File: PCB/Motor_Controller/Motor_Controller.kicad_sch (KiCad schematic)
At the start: 6 parts, among them J1 Motor, Q1 FQD50N06

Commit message: PCB and PWM Update
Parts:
- added D2: IR204A, LED_THT:LED_D3.0mm_IRBlack, symbol LED:IR204A
- added U1: QSE159, OptoDevice:ONSemi_QSE15x, symbol Interface_Optical:QSE159
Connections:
- net GND: now also R2.2; no longer Q1.3 (S), R1.2
- net VIN_12V: now also D1.1 (K), J1.1 (Pin_1); no longer R2.1
- new net ISENSE: Q1.3 (S), R1.2, R2.1
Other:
- moved on the sheet: R2

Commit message: PCB Update
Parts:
- added U2: CH32V003FxPx, Package_SO:TSSOP-20_4.4x6.5mm_P0.65mm, symbol MCU_WCH_CH32V0:CH32V003FxPx
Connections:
- net GND: now also U2.7 (VSS)
- new net CONTROL_POT: U2.20 (PD3)
- new net ISENSE_AMPED: U2.1 (PD4)
- new net MOTOR_PWM: U2.10 (PC0)
- new net NRST: U2.4 (PD7)
- new net VIN_3V3: U2.9 (VDD)

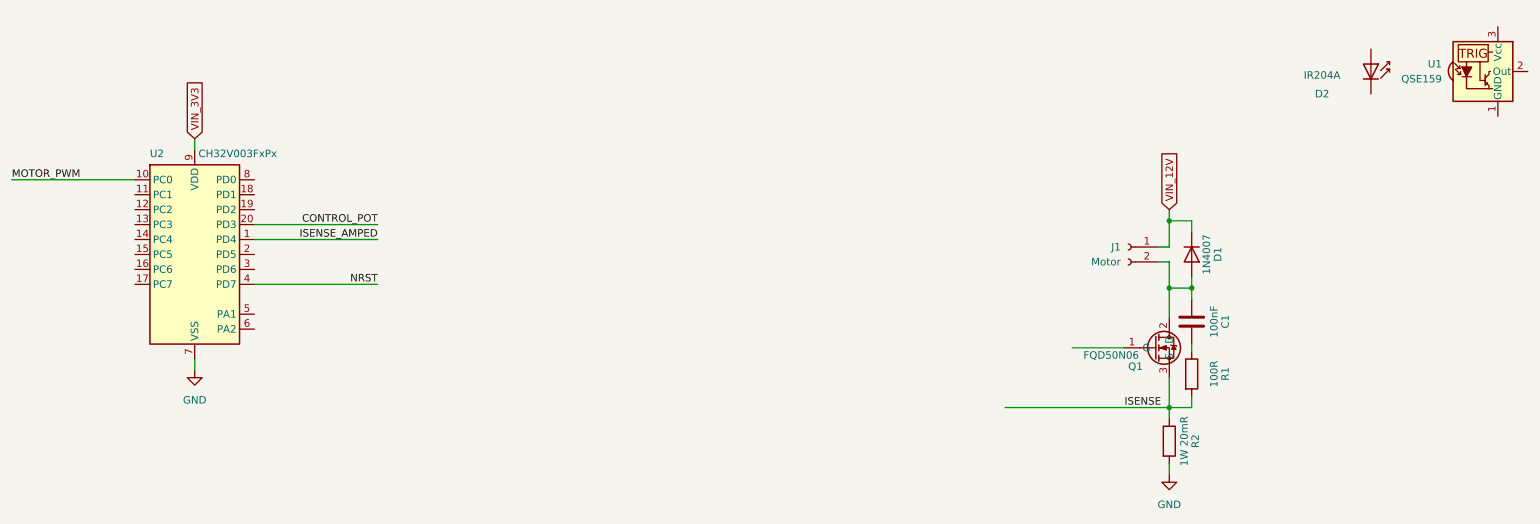
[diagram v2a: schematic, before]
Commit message: Op-Amp Specific Testing
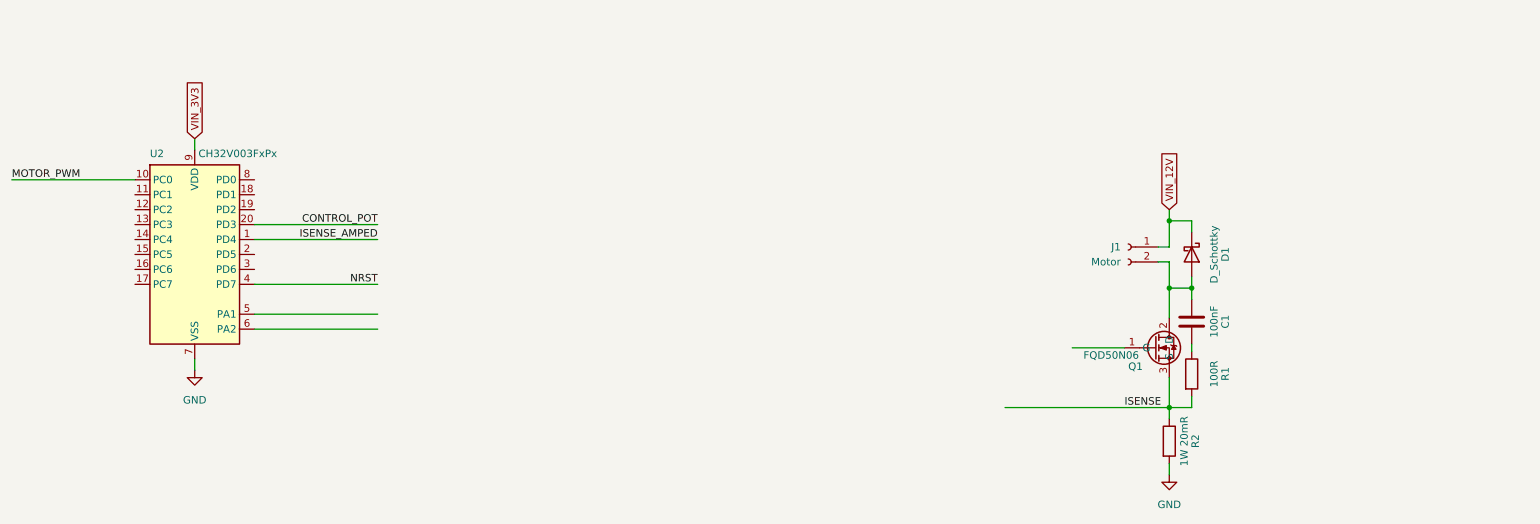
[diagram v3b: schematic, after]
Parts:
- removed D1: 1N4007, symbol Device:D
- removed D2: IR204A, LED_THT:LED_D3.0mm_IRBlack, symbol LED:IR204A
- removed U1: QSE159, OptoDevice:ONSemi_QSE15x, symbol Interface_Optical:QSE159
- added D1: D_Schottky, symbol Device:D_Schottky
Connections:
- net VIN_12V: now also D1.1 (K)
- net at C1.1, J1.2 (Pin_2), Q1.2 (D): now also D1.2 (A)
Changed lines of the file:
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@@
+	(wire
+		(pts
+			(xy 66.04 67.945) (xy 86.995 67.945)
+		)
+		(stroke
+			(width 0)
+			(type default)
+		)
+	)
 	(wire
 		(pts
@@
 		(pts
 			(xy 225.425 51.435) (xy 225.425 49.53)
+		)
+		(stroke
+			(width 0)
+			(type default)
+		)
+	)
+	(wire
+		(pts
+			(xy 66.04 65.405) (xy 86.995 65.405)
 		)
 		(stroke
@@
 	)
 	(symbol
-		(lib_id "Interface_Optical:QSE159")
-		(at 274.955 24.13 0)
-		(unit 1)
-		(exclude_from_sim no)
-		(in_bom yes)
-		(on_board yes)
-		(dnp no)
-		(fields_autoplaced yes)
-		(property "Reference" "U1"
-			(at 267.97 22.8599 0)
-			(effects
-				(font
-					(size 1.27 1.27)
-				)
-				(justify right)
-			)
-		)
-		(property "Value" "QSE159"
-			(at 267.97 25.3999 0)
-			(effects
-				(font
-					(size 1.27 1.27)
-				)
-				(justify right)
-			)
-		)
-		(property "Footprint" "OptoDevice:ONSemi_QSE15x"
-			(at 274.955 34.29 0)
-			(effects
-				(font
-					(size 1.27 1.27)
-				)
-				(hide yes)
-			)
-		)
-		(property "Datasheet" "http://www.onsemi.com/pub/Collateral/QSE159-D.pdf"
-			(at 291.465 16.51 0)
-			(effects
-				(font
-					(size 1.27 1.27)
-				)
-				(hide yes)
-			)
-		)
-		(property "Description" "Plastic Silicon Photosensor"
-			(at 274.955 24.13 0)
-			(effects
-				(font
-					(size 1.27 1.27)
-				)
-				(hide yes)
-			)
-		)
-		(pin "3"
-		)
-		(pin "1"
-		)
-		(pin "2"
-		)
-		(instances
-			(project ""
-				(path "/75427121-ba70-43d0-b78e-325c2cfaa959"
-					(reference "U1")
-					(unit 1)
-				)
-			)
-		)
-	)
-	(symbol
-		(lib_id "Device:D")
-		(at 225.425 55.245 270)
-		(unit 1)
-		(exclude_from_sim no)
-		(in_bom yes)
-		(on_board yes)
-		(dnp no)
-		(property "Reference" "D1"
-			(at 229.87 55.245 0)
-			(effects
-				(font
-					(size 1.27 1.27)
-				)
-			)
-		)
-		(property "Value" "1N4007"
-			(at 227.965 55.245 0)
-			(effects
-				(font
-					(size 1.27 1.27)
-				)
-			)
-		)
-		(property "Footprint" ""
-			(at 225.425 55.245 0)
-			(effects
-				(font
-					(size 1.27 1.27)
-				)
-				(hide yes)
-			)
-		)
-		(property "Datasheet" "~"
-			(at 225.425 55.245 0)
-			(effects
-				(font
-					(size 1.27 1.27)
-				)
-				(hide yes)
-			)
-		)
-		(property "Description" "Diode"
-			(at 225.425 55.245 0)
-			(effects
-				(font
-					(size 1.27 1.27)
-				)
-				(hide yes)
-			)
-		)
-		(property "Sim.Device" "D"
-			(at 225.425 55.245 0)
-			(effects
-				(font
-					(size 1.27 1.27)
-				)
-				(hide yes)
-			)
-		)
-		(property "Sim.Pins" "1=K 2=A"
-			(at 225.425 55.245 0)
-			(effects
-				(font
-					(size 1.27 1.27)
-				)
-				(hide yes)
-			)
-		)
-		(pin "1"
-		)
-		(pin "2"
-		)
-		(instances
-			(project ""
-				(path "/75427121-ba70-43d0-b78e-325c2cfaa959"
-					(reference "D1")
-					(unit 1)
-				)
-			)
-		)
-	)
-	(symbol
 		(lib_id "Connector:Conn_01x02_Socket")
 		(at 214.63 53.975 0)
@@
 	)
 	(symbol
-		(lib_id "LED:IR204A")
-		(at 255.905 22.86 270)
-		(mirror x)
+		(lib_id "Device:D_Schottky")
+		(at 225.425 55.245 270)
 		(unit 1)
 		(exclude_from_sim no)
@@
 		(on_board yes)
 		(dnp no)
-		(property "Reference" "D2"
-			(at 246.38 27.94 90)
-			(effects
-				(font
-					(size 1.27 1.27)
-				)
-				(justify left)
-			)
-		)
-		(property "Value" "IR204A"
-			(at 244.475 24.765 90)
-			(effects
-				(font
-					(size 1.27 1.27)
-				)
-				(justify left)
-			)
-		)
-		(property "Footprint" "LED_THT:LED_D3.0mm_IRBlack"
-			(at 260.35 22.86 0)
-			(effects
-				(font
-					(size 1.27 1.27)
-				)
-				(hide yes)
-			)
-		)
-		(property "Datasheet" "http://www.everlight.com/file/ProductFile/IR204-A.pdf"
-			(at 255.905 24.13 0)
-			(effects
-				(font
-					(size 1.27 1.27)
-				)
-				(hide yes)
-			)
-		)
-		(property "Description" "Infrared LED , 3mm LED package"
-			(at 255.905 22.86 0)
-			(effects
-				(font
-					(size 1.27 1.27)
-				)
-				(hide yes)
-			)
+		(property "Reference" "D1"
+			(at 231.14 55.245 0)
+			(effects
+				(font
+					(size 1.27 1.27)
+				)
+			)
+		)
+		(property "Value" "D_Schottky"
+			(at 229.235 55.245 0)
+			(effects
+				(font
+					(size 1.27 1.27)
+				)
+			)
+		)
+		(property "Footprint" ""
+			(at 225.425 55.245 0)
+			(effects
+				(font
+					(size 1.27 1.27)
+				)
+				(hide yes)
+			)
+		)
+		(property "Datasheet" "~"
+			(at 225.425 55.245 0)
+			(effects
+				(font
+					(size 1.27 1.27)
+				)
+				(hide yes)
+			)
+		)
+		(property "Description" "Schottky diode"
+			(at 225.425 55.245 0)
+			(effects
+				(font
+					(size 1.27 1.27)
+				)
+				(hide yes)
+			)
+		)
+		(pin "1"
 		)
 		(pin "2"
-		)
-		(pin "1"
 		)
 		(instances
 			(project ""
 				(path "/75427121-ba70-43d0-b78e-325c2cfaa959"
-					(reference "D2")
+					(reference "D1")
 					(unit 1)
 				)

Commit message: Added Op Amp code
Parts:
- added R3: 4K7, symbol Device:R
- added R4: 220R, symbol Device:R
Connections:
- net GND: now also R4.2
- net ISENSE_AMPED: now also R3.1
- net at U2.5 (PA1): now also R3.2, R4.1
- net ISENSE_LV: now reaches U2.6 (PA2)
- net ISENSE: no longer names the net of Q1.3 (S), R1.2, R2.1

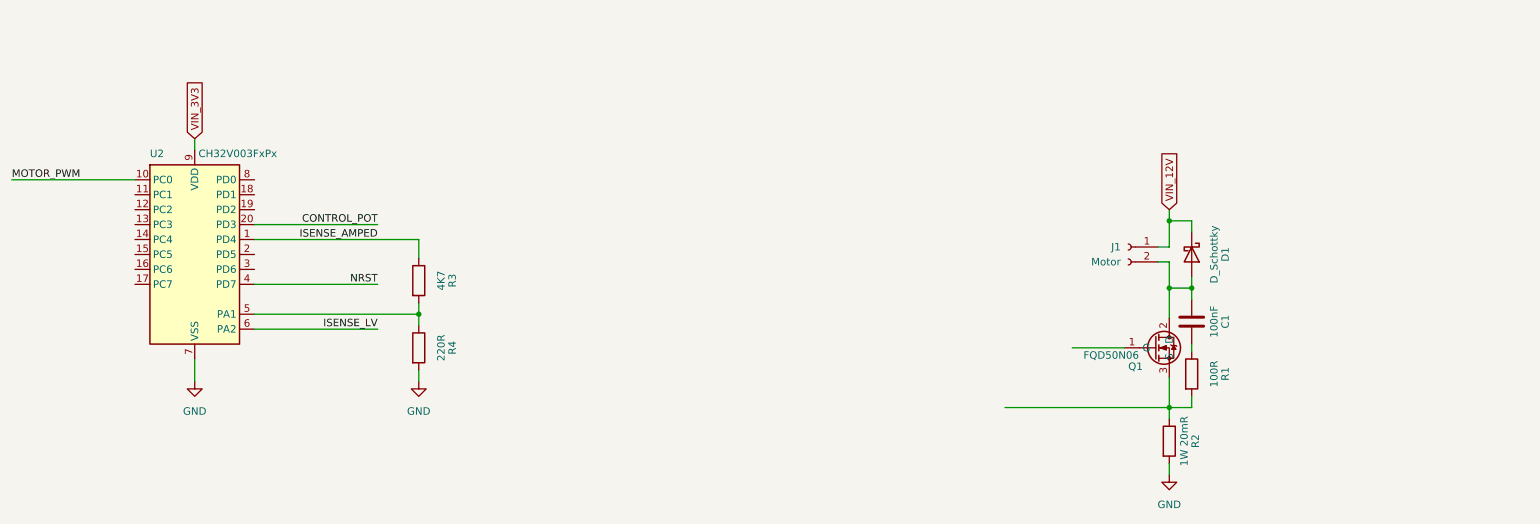
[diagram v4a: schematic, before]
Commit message: Removed Mosfet Driver. Using discreet Push-Pull
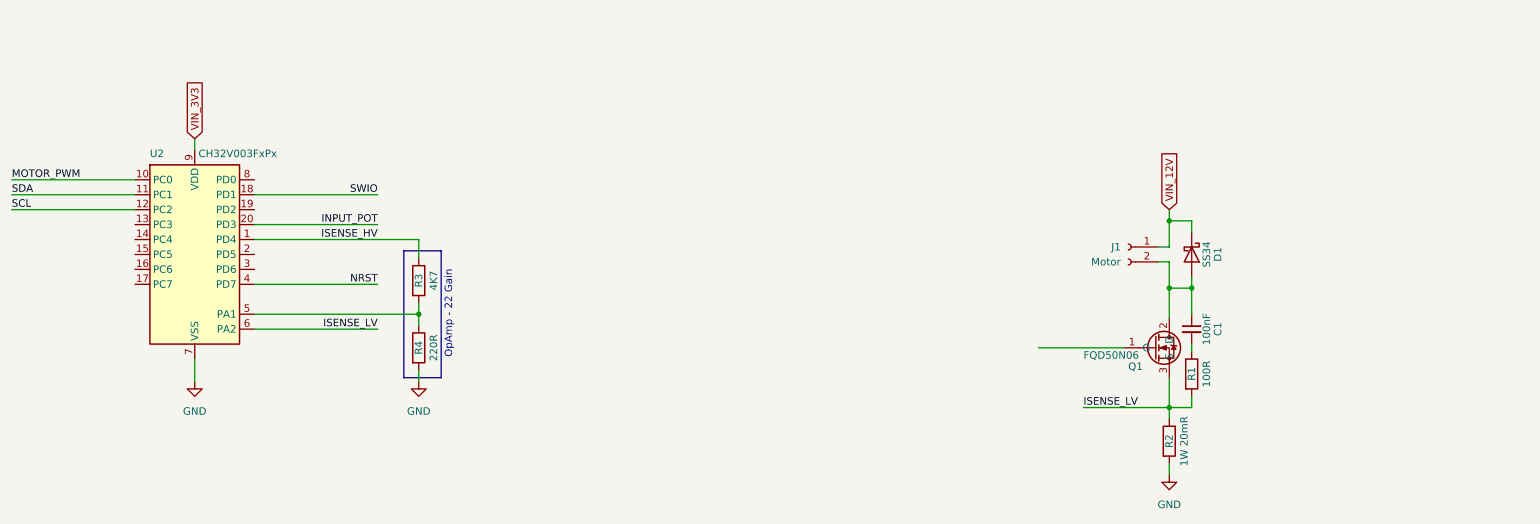
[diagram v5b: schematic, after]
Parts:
- removed C1: 100nF, symbol Device:C
- removed D1: D_Schottky, symbol Device:D_Schottky
- added C1: 100nF, symbol Device:C_Small
- added D1: SS34, Diode_SMD:D_SMA, symbol Diode:SS34
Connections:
- net ISENSE_LV: now also Q1.3 (S), R1.2, R2.1
- net VIN_12V: now also D1.1 (K)
- net at J1.2 (Pin_2), Q1.2 (D): now also C1.1, D1.2 (A)
- net at R1.1: now also C1.2
- net SDA: now reaches U2.11 (PC1)
- net SCL: now reaches U2.12 (PC2)
- net SWIO: now reaches U2.18 (PD1)
- net CONTROL_POT renamed INPUT_POT
- net ISENSE_AMPED renamed ISENSE_HV
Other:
- note added: "OpAmp - 22 Gain"

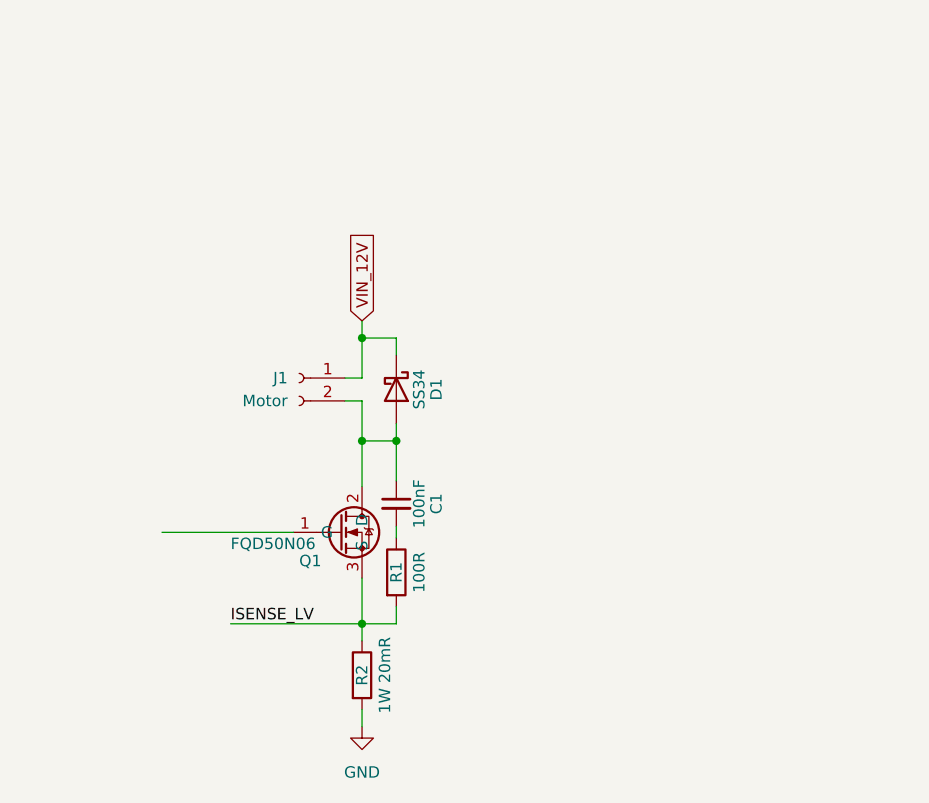
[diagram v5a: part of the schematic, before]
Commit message: Added BJT Drive Circuit
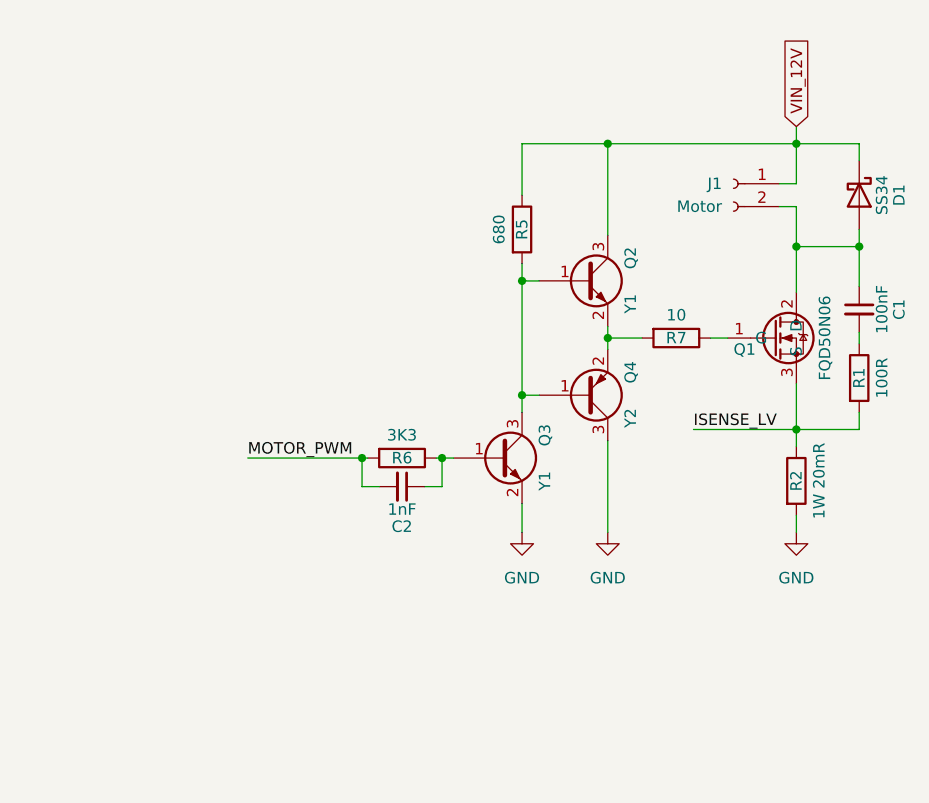
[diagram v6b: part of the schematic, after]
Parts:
- added C2: 1nF, symbol Device:C_Small
- added Q2, Q3: Y1, symbol Device:Q_NPN_BEC
- added Q4: Y2, symbol Device:Q_PNP_BEC
- added R5: 680, symbol Device:R
- added R6: 3K3, symbol Device:R
- added R7: 10, symbol Device:R
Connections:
- net GND: now also Q3.2 (E), Q4.3 (C)
- net MOTOR_PWM: now also C2.2, R6.2
- net VIN_12V: now also Q2.3 (C), R5.1
- net at Q1.1 (G): now also R7.1
- new net: Q2.1 (B), Q3.3 (C), Q4.1 (B), R5.2
- new net: Q2.2 (E), Q4.2 (E), R7.2
- new net: C2.1, Q3.1 (B), R6.1
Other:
- moved on the sheet: C1, D1, J1, Q1, R1, R2
